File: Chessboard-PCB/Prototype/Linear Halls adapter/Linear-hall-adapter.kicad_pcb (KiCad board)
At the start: 2 copper layers, 221 x 101 mm, 0 parts

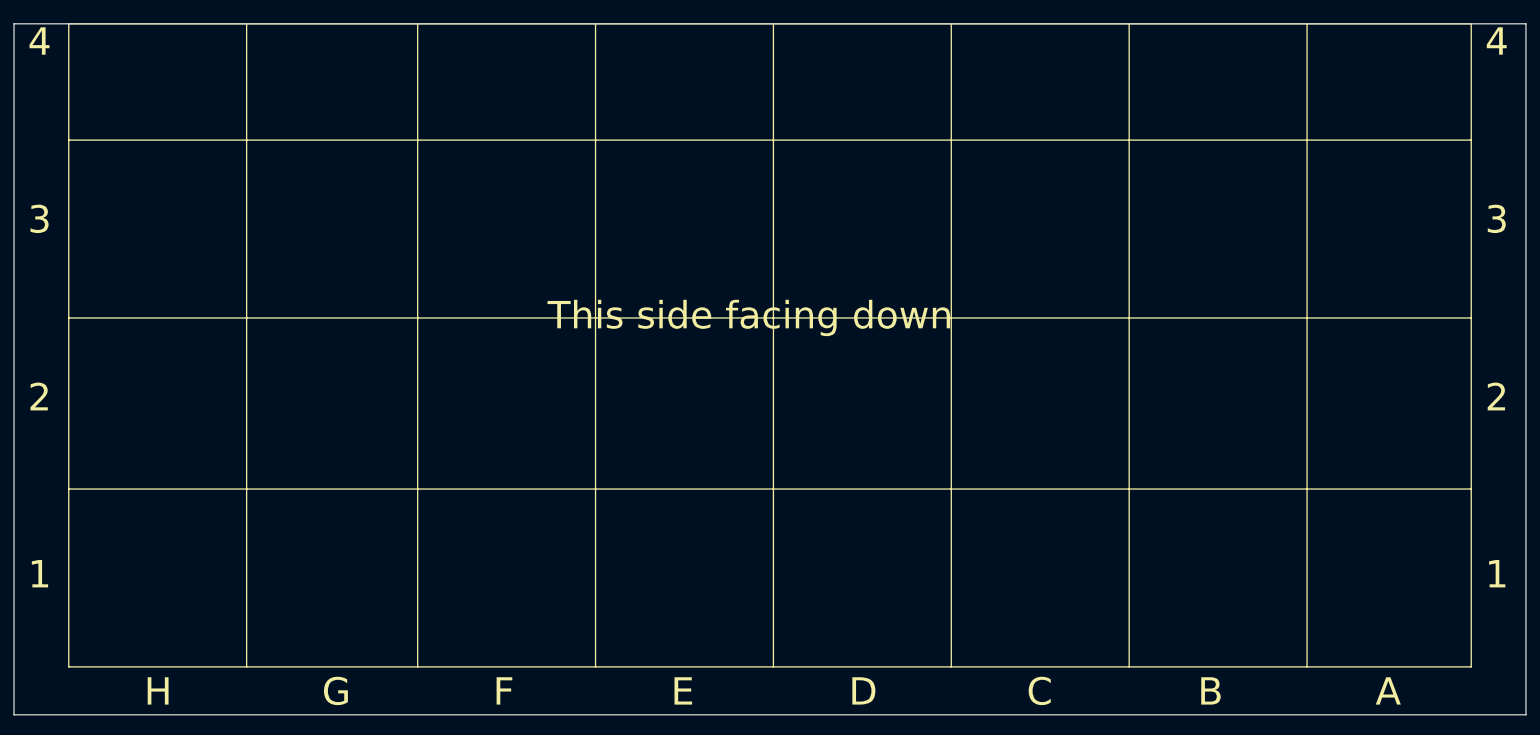
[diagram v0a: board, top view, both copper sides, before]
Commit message: Add SS49Es to PCB
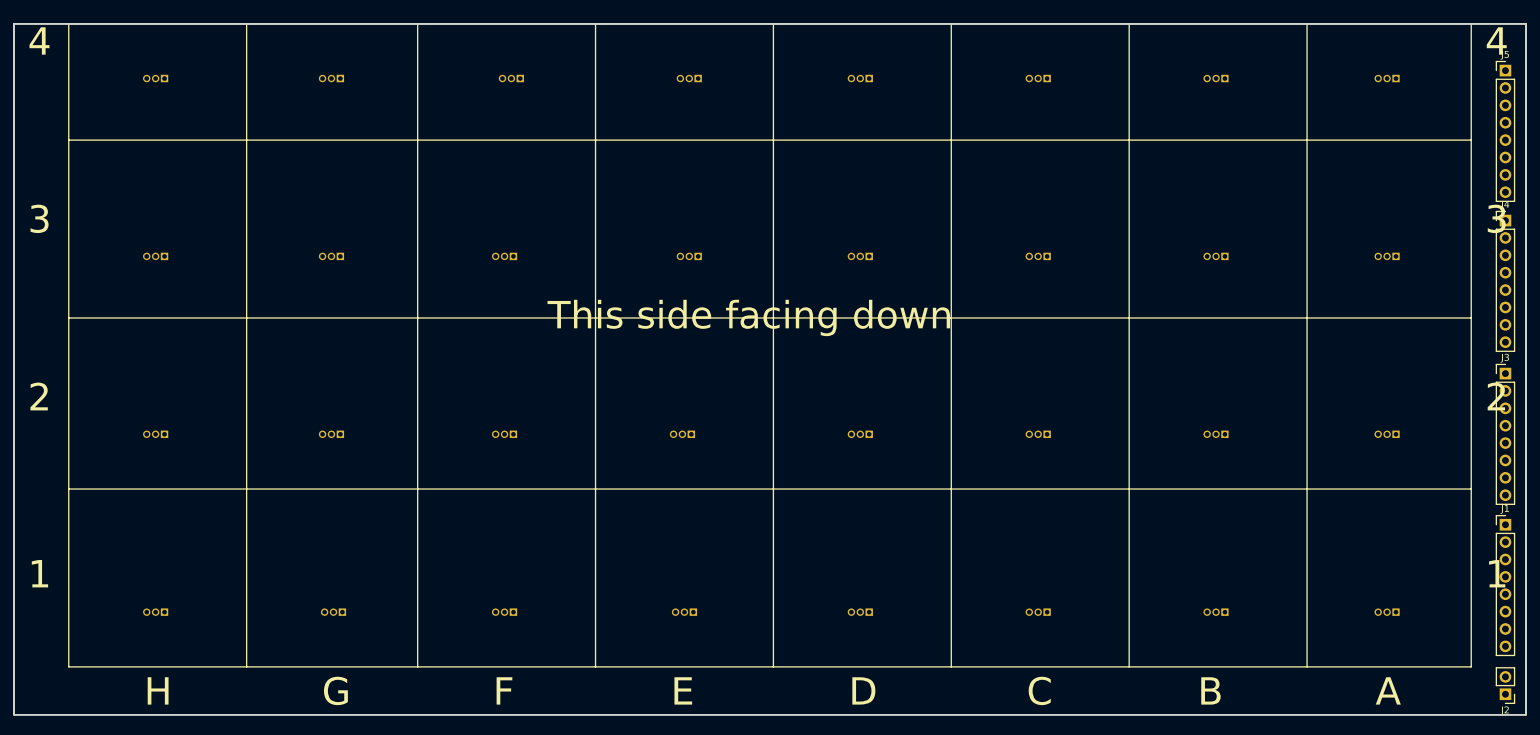
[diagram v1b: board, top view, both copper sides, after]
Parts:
- added IC1: SS49E, SamacSys_Parts:TO130P160X410X300-3P, B.Cu at (42.0, 106.0)
- added IC10: SS49E, SamacSys_Parts:TO130P160X410X300-3P, B.Cu at (67.7, 80.0)
- added IC11: SS49E, SamacSys_Parts:TO130P160X410X300-3P, B.Cu at (93.0, 80.0)
- added IC12: SS49E, SamacSys_Parts:TO130P160X410X300-3P, B.Cu at (119.0, 80.0)
- added IC13: SS49E, SamacSys_Parts:TO130P160X410X300-3P, B.Cu at (145.0, 80.0)
- added IC14: SS49E, SamacSys_Parts:TO130P160X410X300-3P, B.Cu at (171.0, 80.0)
- added IC15: SS49E, SamacSys_Parts:TO130P160X410X300-3P, B.Cu at (197.0, 80.0)
- added IC16: SS49E, SamacSys_Parts:TO130P160X410X300-3P, B.Cu at (222.0, 80.0)
- added IC17: SS49E, SamacSys_Parts:TO130P160X410X300-3P, B.Cu at (42.0, 54.0)
- added IC18: SS49E, SamacSys_Parts:TO130P160X410X300-3P, B.Cu at (67.7, 54.0)
- added IC19: SS49E, SamacSys_Parts:TO130P160X410X300-3P, B.Cu at (93.0, 54.0)
- added IC2: SS49E, SamacSys_Parts:TO130P160X410X300-3P, B.Cu at (68.0, 106.0)
- added IC20: SS49E, SamacSys_Parts:TO130P160X410X300-3P, B.Cu at (120.0, 54.0)
- added IC21: SS49E, SamacSys_Parts:TO130P160X410X300-3P, B.Cu at (145.0, 54.0)
- added IC22: SS49E, SamacSys_Parts:TO130P160X410X300-3P, B.Cu at (171.0, 54.0)
- added IC23: SS49E, SamacSys_Parts:TO130P160X410X300-3P, B.Cu at (197.0, 54.0)
- added IC24: SS49E, SamacSys_Parts:TO130P160X410X300-3P, B.Cu at (222.0, 54.0)
- added IC25: SS49E, SamacSys_Parts:TO130P160X410X300-3P, B.Cu at (42.0, 28.0)
- added IC26: SS49E, SamacSys_Parts:TO130P160X410X300-3P, B.Cu at (67.7, 28.0)
- added IC27: SS49E, SamacSys_Parts:TO130P160X410X300-3P, B.Cu at (94.0, 28.0)
- added IC28: SS49E, SamacSys_Parts:TO130P160X410X300-3P, B.Cu at (120.0, 28.0)
- added IC29: SS49E, SamacSys_Parts:TO130P160X410X300-3P, B.Cu at (145.0, 28.0)
- added IC3: SS49E, SamacSys_Parts:TO130P160X410X300-3P, B.Cu at (93.0, 106.0)
- added IC30: SS49E, SamacSys_Parts:TO130P160X410X300-3P, B.Cu at (171.0, 28.0)
- added IC31: SS49E, SamacSys_Parts:TO130P160X410X300-3P, B.Cu at (197.0, 28.0)
- added IC32: SS49E, SamacSys_Parts:TO130P160X410X300-3P, B.Cu at (222.0, 28.0)
- added IC4: SS49E, SamacSys_Parts:TO130P160X410X300-3P, B.Cu at (119.3, 106.0)
- added IC5: SS49E, SamacSys_Parts:TO130P160X410X300-3P, B.Cu at (145.0, 106.0)
- added IC6: SS49E, SamacSys_Parts:TO130P160X410X300-3P, B.Cu at (171.0, 106.0)
- added IC7: SS49E, SamacSys_Parts:TO130P160X410X300-3P, B.Cu at (197.0, 106.0)
- added IC8: SS49E, SamacSys_Parts:TO130P160X410X300-3P, B.Cu at (222.0, 106.0)
- added IC9: SS49E, SamacSys_Parts:TO130P160X410X300-3P, B.Cu at (42.0, 80.0)
- added J1: Conn_01x08, Connector_PinHeader_2.54mm:PinHeader_1x08_P2.54mm_Vertical, F.Cu at (238.0, 93.2)
- added J2: Conn_01x02, Connector_PinHeader_2.54mm:PinHeader_1x02_P2.54mm_Vertical, F.Cu at (238.0, 118.0)
- added J3: Conn_01x08, Connector_PinHeader_2.54mm:PinHeader_1x08_P2.54mm_Vertical, F.Cu at (238.0, 71.1)
- added J4: Conn_01x08, Connector_PinHeader_2.54mm:PinHeader_1x08_P2.54mm_Vertical, F.Cu at (238.0, 48.8)
- added J5: Conn_01x08, Connector_PinHeader_2.54mm:PinHeader_1x08_P2.54mm_Vertical, F.Cu at (238.0, 26.8)
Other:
- board text added: "This side facing up"
